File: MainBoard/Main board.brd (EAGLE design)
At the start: 100 x 100 mm, 10 parts

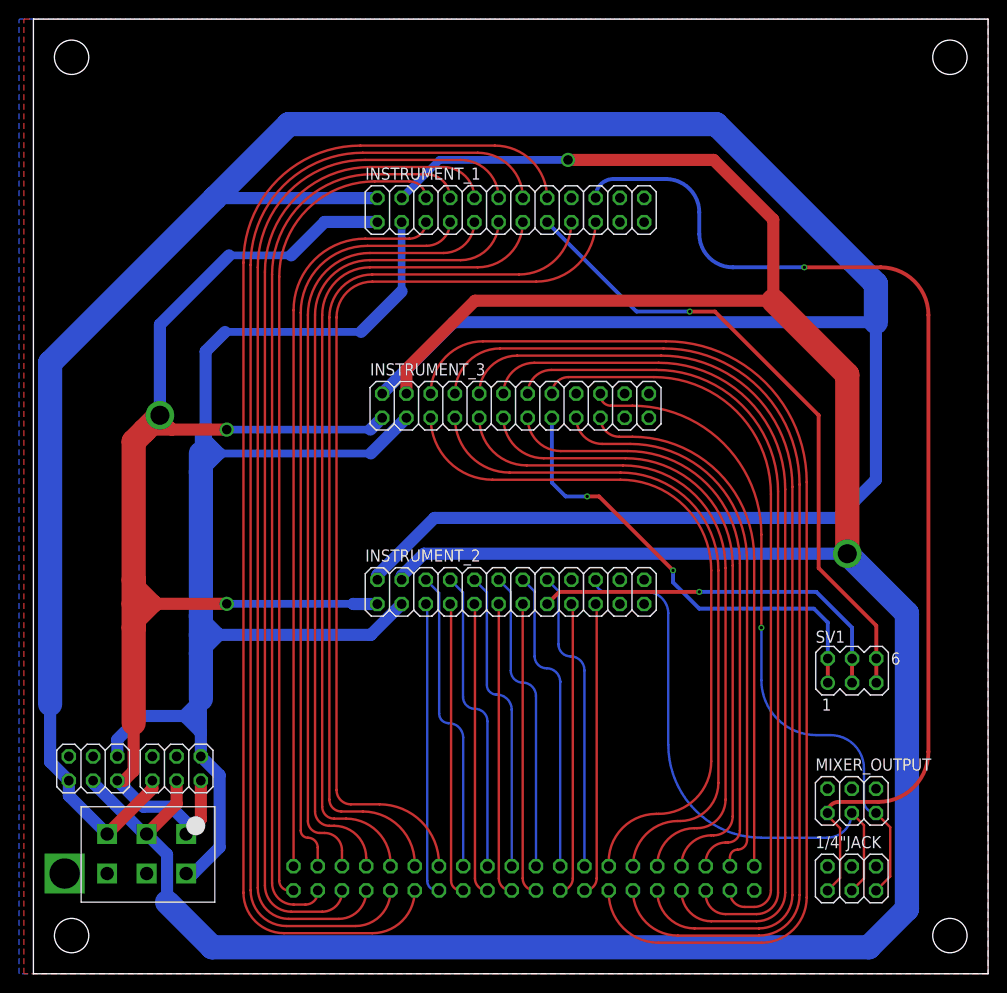
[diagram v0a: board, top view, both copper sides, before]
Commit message: Version 3 of mainboard
Added sequencer pinouts and manually did all traces.
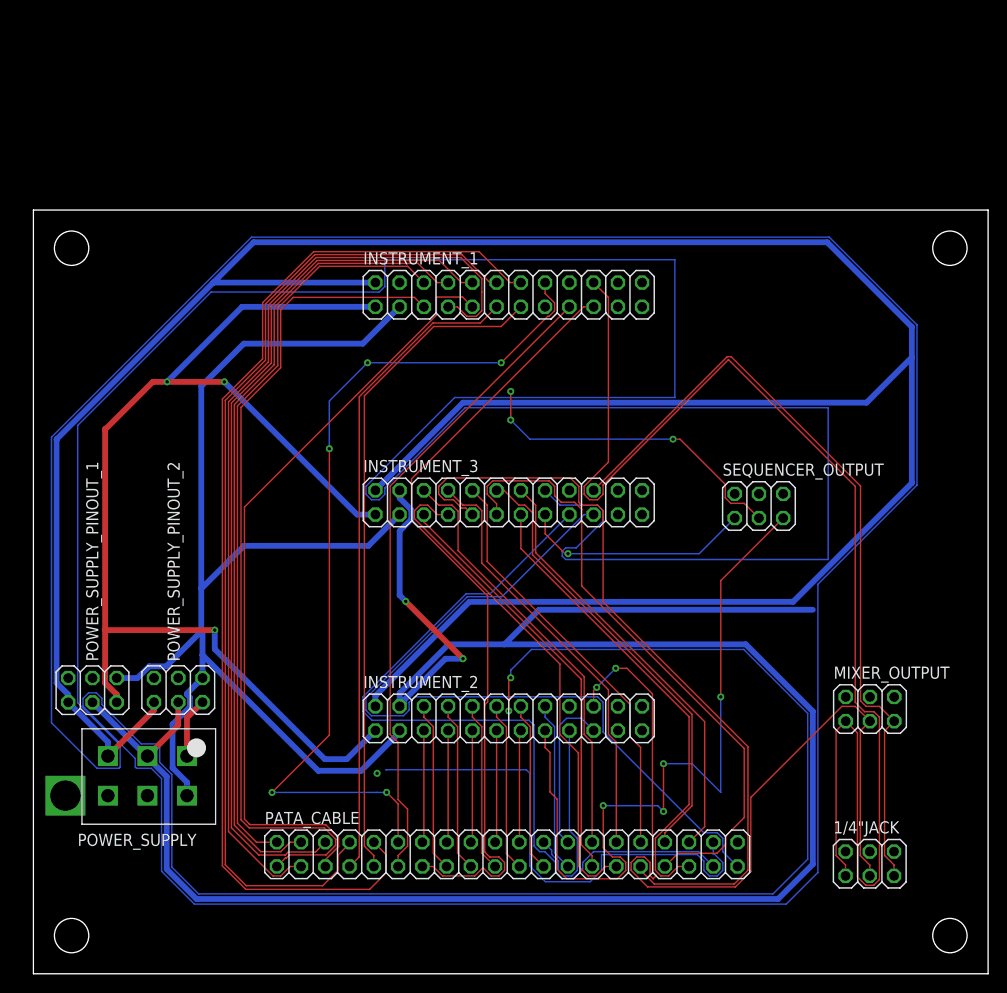
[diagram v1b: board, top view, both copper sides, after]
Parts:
- removed SV1: (no value), con-lstb:MA03-2
- added SEQUENCER_OUTPUT: (no value), pinhead:2X03
- moved INSTRUMENT_2 13.3 mm to (49.8, 26.8)
- moved INSTRUMENT_3 10.2 mm to (49.8, 49.4)
- moved MIXER_OUTPUT 9.81 mm to (87.6, 27.7)
- moved INSTRUMENT_1 8.87 mm to (49.8, 71.1)
- moved POWER_SUPPLY_PINOUT_2 8.22 mm to (15.2, 29.7)
- moved POWER_SUPPLY_PINOUT_1 8.21 mm to (6.19, 29.7)
- moved POWER_SUPPLY 8.16 mm to (16.1, 18.7)
- moved PATA_CABLE 3.05 mm to (49.6, 12.5), flipped to the top, turned to 0 degrees
- moved 1/4"JACK 2.44 mm to (87.6, 11.5)
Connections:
- net DGND renamed DIGITAL_GND
- net OUT1 renamed ANALOG_OUTPUT_1
- net OUT2 renamed ANALOG_OUTPUT_2
- net OUT3 renamed ANALOG_OUTPUT_3
- net SW_2 renamed SWITCH_2
- net SW_3 renamed SWITCH_3
- net SW_4 renamed SWITCH_4
- net SW_5 renamed SWITCH_5
- net SW_6 renamed SWITCH_6
- net SW_7 renamed SWITCH_7
- net SW_8 renamed SWITCH_8
- net SW_9 renamed SWITCH_9
- removed net AGND: 1/4"JACK.2, 1/4"JACK.4, 1/4"JACK.6, INSTRUMENT_1.18, INSTRUMENT_1.22, INSTRUMENT_2.18, INSTRUMENT_2.22, INSTRUMENT_3.18, INSTRUMENT_3.22, MIXER_OUTPUT.2, MIXER_OUTPUT.4, MIXER_OUTPUT.6, PATA_CABLE.40, POWER_SUPPLY.AGND0, POWER_SUPPLY.AGND1, POWER_SUPPLY_PINOUT_1.2, POWER_SUPPLY_PINOUT_1.4, POWER_SUPPLY_PINOUT_2.2, POWER_SUPPLY_PINOUT_2.4
- removed net TRIG1: INSTRUMENT_1.15, SV1.5, SV1.6
- removed net TRIG2: INSTRUMENT_2.15, SV1.3, SV1.4
- removed net TRIG3: INSTRUMENT_3.15, SV1.1, SV1.2
- new net ANALOG_GND: 1/4"JACK.2, 1/4"JACK.4, 1/4"JACK.6, INSTRUMENT_1.18, INSTRUMENT_1.22, INSTRUMENT_2.18, INSTRUMENT_2.22, INSTRUMENT_3.18, INSTRUMENT_3.22, POWER_SUPPLY.AGND0, POWER_SUPPLY.AGND1, POWER_SUPPLY_PINOUT_1.2, POWER_SUPPLY_PINOUT_1.4, POWER_SUPPLY_PINOUT_2.2, POWER_SUPPLY_PINOUT_2.4, SEQUENCER_OUTPUT.2, SEQUENCER_OUTPUT.4, SEQUENCER_OUTPUT.6
- new net GND: MIXER_OUTPUT.6
- new net N$1: SEQUENCER_OUTPUT.3
- new net SEQUENCER_TRIGGER: INSTRUMENT_1.15, INSTRUMENT_2.15, INSTRUMENT_3.15, SEQUENCER_OUTPUT.1, SEQUENCER_OUTPUT.5
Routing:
- net SWITCH_7: track 76.1 -> 770.6 mm, vias 0 -> 2
- net SEQUENCER_TRIGGER: track 0.00 -> 105.8 mm, vias 0 -> 5
- net -12V: track 317.3 -> 227.9 mm
- net POT_11B: track 116.4 -> 45.0 mm
- net TRIG1: track 67.3 -> 0.00 mm, vias 1 -> 0
- net POT_12B: track 108.1 -> 45.0 mm
- net POT_13B: track 100.2 -> 44.2 mm
- net TRIG3: track 48.8 -> 0.00 mm, vias 2 -> 0
- net POT_14B: track 92.1 -> 47.3 mm
- net TRIG2: track 39.8 -> 0.00 mm, vias 1 -> 0
- net POT_15B: track 84.3 -> 45.5 mm
- net SWITCH_1: track 126.7 -> 92.1 mm, vias 0 -> 5
- net N$1: track 0.00 -> 34.1 mm, vias 0 -> 3
- net ANALOG_OUTPUT_2: track 56.4 -> 90.5 mm, vias 0 -> 2
- net ANALOG_OUTPUT_1: track 111.2 -> 144.2 mm, vias 1 -> 0
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- removed copper zone on layer 1, net AGND
- removed copper zone on layer 16, net AGND
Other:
- board size 100 x 100 mm -> 100 x 80 mm

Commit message: Version 4
Added ground traces to previous version.
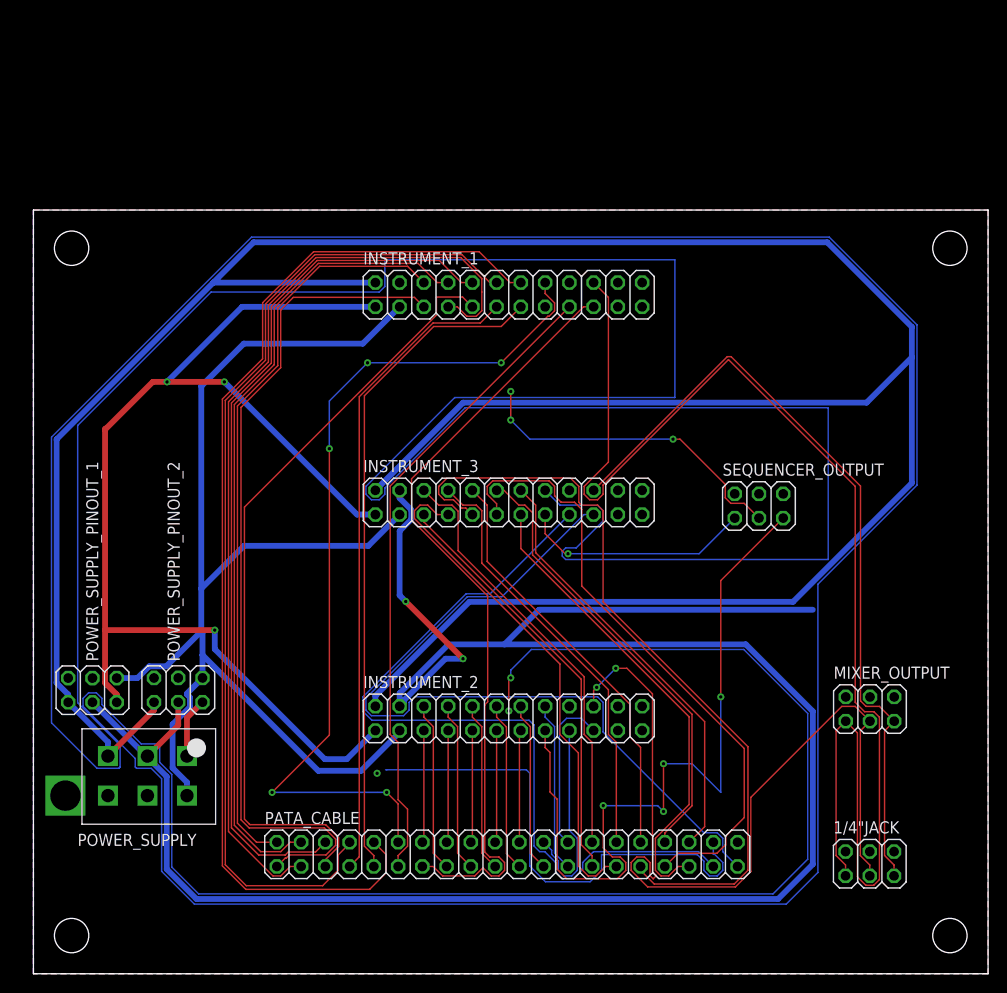
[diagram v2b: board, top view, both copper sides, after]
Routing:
- added copper zone on layer 1, net ANALOG_GND
- added copper zone on layer 16, net DIGITAL_GND
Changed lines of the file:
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@@
 <contactref element="SEQUENCER_OUTPUT" pad="4"/>
 <contactref element="SEQUENCER_OUTPUT" pad="2"/>
-<wire x1="56.14" y1="72.4" x2="61.22" y2="72.4" width="0" layer="19" extent="1-1"/>
+<polygon width="0.1524" layer="1">
+<vertex x="0" y="0"/>
+<vertex x="0" y="80"/>
+<vertex x="100" y="80"/>
+<vertex x="100" y="0"/>
+</polygon>
+<wire x1="87.607675" y1="12.798159375" x2="90.147675" y2="12.798159375" width="0" layer="19" extent="1-1"/>
+<wire x1="85.067675" y1="12.798159375" x2="87.607675" y2="12.798159375" width="0" layer="19" extent="1-1"/>
 <wire x1="61.22" y1="50.64" x2="61.22" y2="72.4" width="0" layer="19" extent="1-1"/>
 <wire x1="56.14" y1="50.64" x2="61.22" y2="50.64" width="0" layer="19" extent="1-1"/>
 <wire x1="61.22" y1="28.02" x2="61.22" y2="50.64" width="0" layer="19" extent="1-1"/>
 <wire x1="56.14" y1="28.02" x2="61.22" y2="28.02" width="0" layer="19" extent="1-1"/>
-<wire x1="85.067675" y1="12.798159375" x2="61.22" y2="28.02" width="0" layer="19" extent="1-1"/>
-<wire x1="87.607675" y1="12.798159375" x2="85.067675" y2="12.798159375" width="0" layer="19" extent="1-1"/>
-<wire x1="90.147675" y1="12.798159375" x2="87.607675" y2="12.798159375" width="0" layer="19" extent="1-1"/>
-<wire x1="15.1718625" y1="30.986634375" x2="56.14" y2="28.02" width="0" layer="19" extent="1-1"/>
-<wire x1="12.6318625" y1="30.986634375" x2="15.1718625" y2="30.986634375" width="0" layer="19" extent="1-1"/>
-<wire x1="6.185453125" y1="30.9749" x2="12.6318625" y2="30.986634375" width="0" layer="19" extent="1-1"/>
-<wire x1="3.645453125" y1="30.9749" x2="6.185453125" y2="30.9749" width="0" layer="19" extent="1-1"/>
-<wire x1="11.9440625" y1="18.662021875" x2="12.6318625" y2="30.986634375" width="0" layer="19" extent="1-1"/>
-<wire x1="7.8040625" y1="18.662021875" x2="11.9440625" y2="18.662021875" width="0" layer="19" extent="1-1"/>
-<wire x1="78.54" y1="50.27" x2="7.8040625" y2="18.662021875" width="0" layer="19" extent="1-1"/>
-<wire x1="76" y1="50.27" x2="78.54" y2="50.27" width="0" layer="19" extent="1-1"/>
-<wire x1="73.46" y1="50.27" x2="76" y2="50.27" width="0" layer="19" extent="1-1"/>
 </signal>
 <signal name="DIGITAL_GND">
@@
 <wire x1="38.36" y1="25.48" x2="38.36" y2="25.2957875" width="0.6096" layer="16"/>
 <wire x1="38.36" y1="25.2957875" x2="34.3250125" y2="21.2608" width="0.6096" layer="16"/>
+<polygon width="0.1524" layer="16">
+<vertex x="0" y="0"/>
+<vertex x="0" y="80"/>
+<vertex x="100" y="80"/>
+<vertex x="100" y="0"/>
+</polygon>
 </signal>
 <signal name="+5V">
@@
 <wire x1="32.82" y1="22.48" x2="35.82" y2="25.48" width="0.6096" layer="16"/>
 <wire x1="32.82" y1="22.48" x2="30.52" y2="22.48" width="0.6096" layer="16"/>
-<wire x1="8.725453125" y1="28.4349" x2="16.0840625" y2="26.818834375" width="0" layer="19" extent="1-1"/>
+<wire x1="19" y1="34" x2="17.7118625" y2="28.446634375" width="0" layer="19" extent="16-16"/>
 <wire x1="3.3540625" y1="18.662021875" x2="8.725453125" y2="28.4349" width="0" layer="19" extent="1-1"/>
 </signal>

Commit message: This board should work
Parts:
- removed SEQUENCER_OUTPUT: (no value), pinhead:2X03
- added TRIG_IN: (no value), con-lstb:MA03-2
- moved INSTRUMENT_2 13.3 mm to (50.0, 40.0)
- moved INSTRUMENT_3 10.2 mm to (50.5, 59.5)
- moved MIXER_OUTPUT 9.81 mm to (85.7, 18.1)
- moved INSTRUMENT_1 8.87 mm to (50.0, 80.0)
- moved POWER_SUPPLY_PINOUT_2 8.22 mm to (15.0, 21.5)
- moved POWER_SUPPLY_PINOUT_1 8.21 mm to (6.25, 21.5)
- moved POWER_SUPPLY 8.16 mm to (16.0, 10.5)
- moved PATA_CABLE 3.05 mm to (51.4, 10.0), flipped to the bottom, turned to 180 degrees
- moved 1/4"JACK 2.44 mm to (85.7, 9.98)
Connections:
- net ANALOG_OUTPUT_1 renamed OUT1
- net ANALOG_OUTPUT_2 renamed OUT2
- net ANALOG_OUTPUT_3 renamed OUT3
- net DIGITAL_GND renamed DGND
- net SWITCH_2 renamed SW_2
- net SWITCH_3 renamed SW_3
- net SWITCH_4 renamed SW_4
- net SWITCH_5 renamed SW_5
- net SWITCH_6 renamed SW_6
- net SWITCH_7 renamed SW_7
- net SWITCH_8 renamed SW_8
- net SWITCH_9 renamed SW_9
- removed net ANALOG_GND: 1/4"JACK.2, 1/4"JACK.4, 1/4"JACK.6, INSTRUMENT_1.18, INSTRUMENT_1.22, INSTRUMENT_2.18, INSTRUMENT_2.22, INSTRUMENT_3.18, INSTRUMENT_3.22, POWER_SUPPLY.AGND0, POWER_SUPPLY.AGND1, POWER_SUPPLY_PINOUT_1.2, POWER_SUPPLY_PINOUT_1.4, POWER_SUPPLY_PINOUT_2.2, POWER_SUPPLY_PINOUT_2.4, SEQUENCER_OUTPUT.2, SEQUENCER_OUTPUT.4, SEQUENCER_OUTPUT.6
- removed net GND: MIXER_OUTPUT.6
- removed net N$1: SEQUENCER_OUTPUT.3
- removed net SEQUENCER_TRIGGER: INSTRUMENT_1.15, INSTRUMENT_2.15, INSTRUMENT_3.15, SEQUENCER_OUTPUT.1, SEQUENCER_OUTPUT.5
- new net AGND: 1/4"JACK.2, 1/4"JACK.4, 1/4"JACK.6, INSTRUMENT_1.18, INSTRUMENT_1.22, INSTRUMENT_2.18, INSTRUMENT_2.22, INSTRUMENT_3.18, INSTRUMENT_3.22, MIXER_OUTPUT.2, MIXER_OUTPUT.4, MIXER_OUTPUT.6, PATA_CABLE.40, POWER_SUPPLY.AGND0, POWER_SUPPLY.AGND1, POWER_SUPPLY_PINOUT_1.2, POWER_SUPPLY_PINOUT_1.4, POWER_SUPPLY_PINOUT_2.2, POWER_SUPPLY_PINOUT_2.4
- new net TRIG1: INSTRUMENT_1.15, TRIG_IN.5, TRIG_IN.6
- new net TRIG2: INSTRUMENT_2.15, TRIG_IN.3, TRIG_IN.4
- new net TRIG3: INSTRUMENT_3.15, TRIG_IN.1, TRIG_IN.2
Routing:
- net SW_7: track 770.6 -> 76.1 mm, vias 2 -> 0
- net SEQUENCER_TRIGGER: track 105.8 -> 0.00 mm, vias 5 -> 0
- net -12V: track 227.9 -> 317.3 mm
- net TRIG1: track 0.00 -> 72.1 mm, vias 0 -> 1
- net POT_11B: track 45.0 -> 116.4 mm
- net POT_12B: track 45.0 -> 108.1 mm
- net POT_13B: track 44.2 -> 100.2 mm
- net TRIG3: track 0.00 -> 53.6 mm, vias 0 -> 2
- net POT_14B: track 47.3 -> 92.1 mm
- net TRIG2: track 0.00 -> 44.5 mm, vias 0 -> 1
- net POT_15B: track 45.5 -> 84.3 mm
- net SWITCH_1: track 92.1 -> 126.7 mm, vias 5 -> 0
- net N$1: track 34.1 -> 0.00 mm, vias 3 -> 0
- net OUT2: track 90.5 -> 56.4 mm, vias 2 -> 0
- net OUT1: track 144.2 -> 111.2 mm, vias 0 -> 1
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- added copper zone on layer 1, net AGND
- added copper zone on layer 16, net AGND
- removed copper zone on layer 1, net ANALOG_GND
- removed copper zone on layer 16, net DGND
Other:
- board size 100 x 80 mm -> 100 x 100 mm

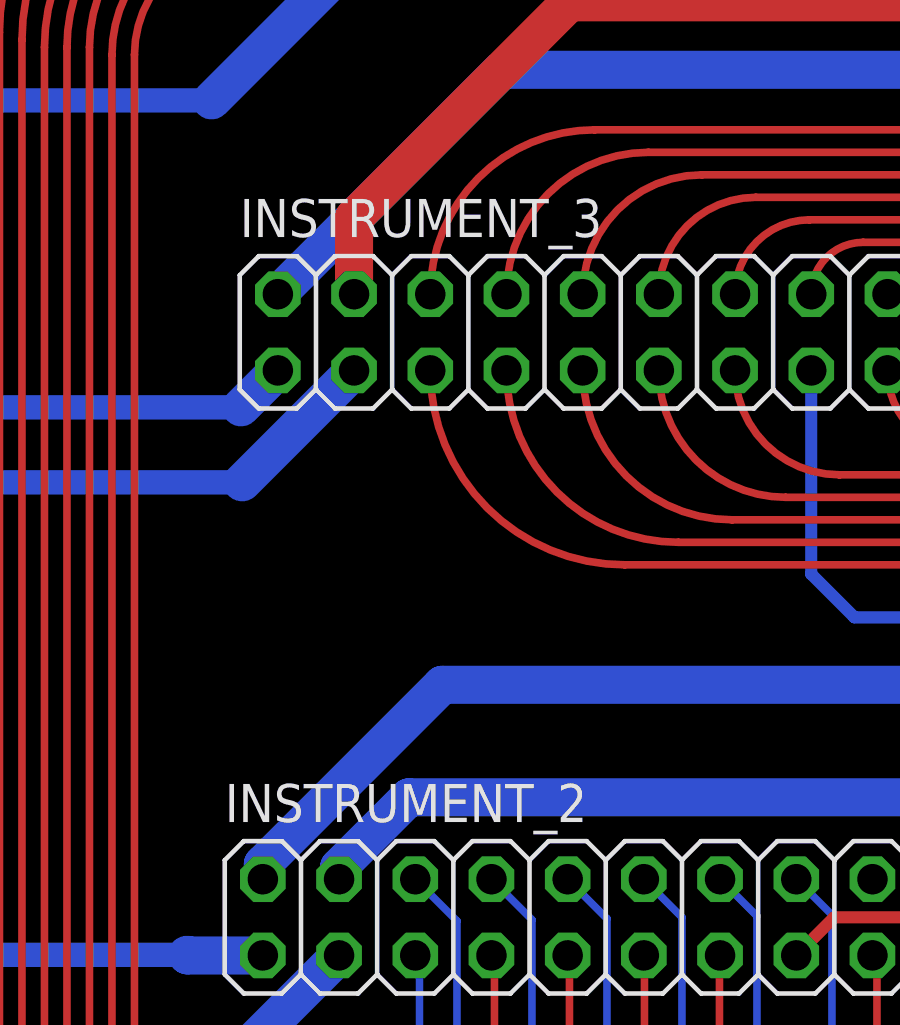
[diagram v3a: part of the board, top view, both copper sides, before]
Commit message: Swapped Instruments 2 and 3
Swapped instruments 2 and 3 so they are in proper order
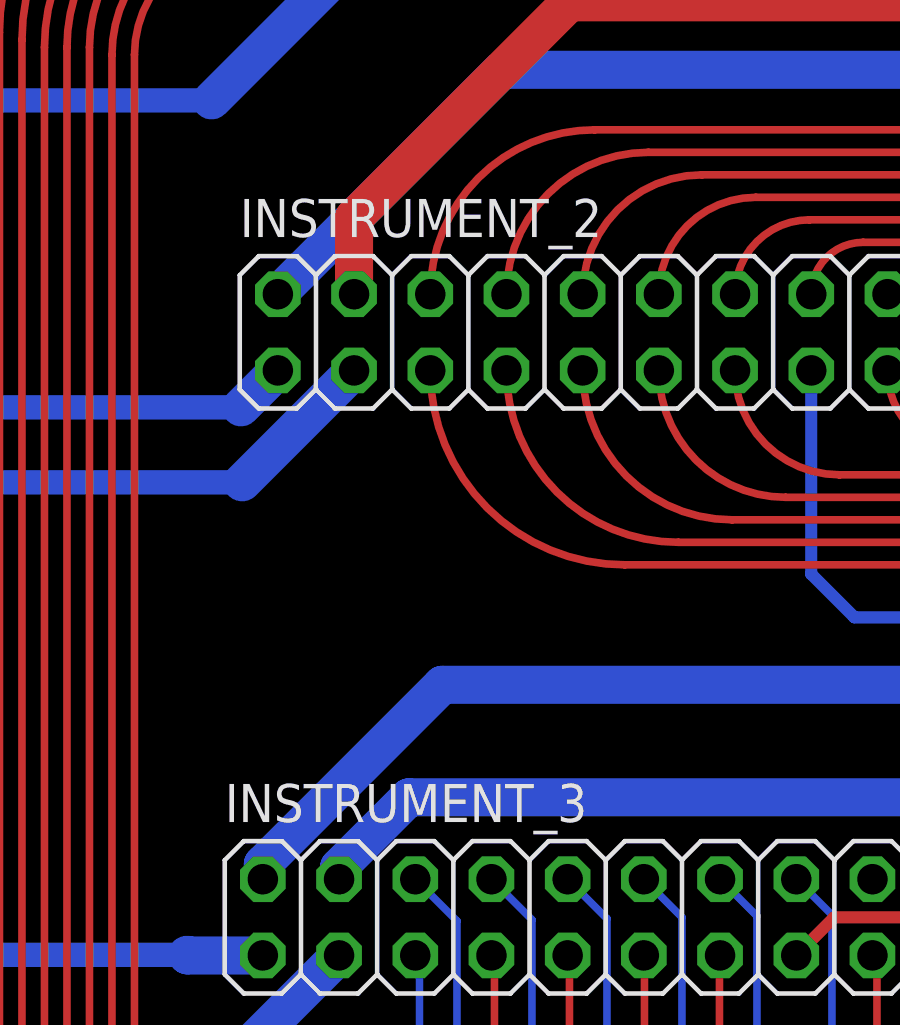
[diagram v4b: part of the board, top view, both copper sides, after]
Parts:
- moved INSTRUMENT_2 19.5 mm to (50.5, 59.5)
- moved INSTRUMENT_3 19.5 mm to (50.0, 40.0)
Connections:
- net OUT2: now also INSTRUMENT_3.20; no longer INSTRUMENT_2.20
- net OUT3: now also INSTRUMENT_2.20; no longer INSTRUMENT_3.20
- net POT_10A: now also INSTRUMENT_3.13; no longer INSTRUMENT_2.13
- net POT_10B: now also INSTRUMENT_3.14; no longer INSTRUMENT_2.14
- net POT_11A: now also INSTRUMENT_2.5; no longer INSTRUMENT_3.5
- net POT_11B: now also INSTRUMENT_2.6; no longer INSTRUMENT_3.6
- net POT_12A: now also INSTRUMENT_2.7; no longer INSTRUMENT_3.7
- net POT_12B: now also INSTRUMENT_2.8; no longer INSTRUMENT_3.8
- net POT_13A: now also INSTRUMENT_2.9; no longer INSTRUMENT_3.9
- net POT_13B: now also INSTRUMENT_2.10; no longer INSTRUMENT_3.10
- net POT_14A: now also INSTRUMENT_2.11; no longer INSTRUMENT_3.11
- net POT_14B: now also INSTRUMENT_2.12; no longer INSTRUMENT_3.12
- net POT_15A: now also INSTRUMENT_2.13; no longer INSTRUMENT_3.13
- net POT_15B: now also INSTRUMENT_2.14; no longer INSTRUMENT_3.14
- net POT_6A: now also INSTRUMENT_3.5; no longer INSTRUMENT_2.5
- net POT_6B: now also INSTRUMENT_3.6; no longer INSTRUMENT_2.6
- net POT_7A: now also INSTRUMENT_3.7; no longer INSTRUMENT_2.7
- net POT_7B: now also INSTRUMENT_3.8; no longer INSTRUMENT_2.8
- net POT_8A: now also INSTRUMENT_3.9; no longer INSTRUMENT_2.9
- net POT_8B: now also INSTRUMENT_3.10; no longer INSTRUMENT_2.10
- net POT_9A: now also INSTRUMENT_3.11; no longer INSTRUMENT_2.11
- net POT_9B: now also INSTRUMENT_3.12; no longer INSTRUMENT_2.12
- net SW_4: now also INSTRUMENT_3.16; no longer INSTRUMENT_2.16
- net SW_5: now also INSTRUMENT_3.17; no longer INSTRUMENT_2.17
- net SW_6: now also INSTRUMENT_3.19; no longer INSTRUMENT_2.19
- net SW_7: now also INSTRUMENT_2.16; no longer INSTRUMENT_3.16
- net SW_8: now also INSTRUMENT_2.17; no longer INSTRUMENT_3.17
- net SW_9: now also INSTRUMENT_2.19; no longer INSTRUMENT_3.19
- net TRIG2: now also INSTRUMENT_3.15; no longer INSTRUMENT_2.15
- net TRIG3: now also INSTRUMENT_2.15; no longer INSTRUMENT_3.15
